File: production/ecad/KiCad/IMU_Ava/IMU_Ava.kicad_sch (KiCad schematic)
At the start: 0 parts

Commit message: add schematic, pullup resistors
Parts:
- added C1, C2: 100nF, Capacitor_SMD:C_0805_2012Metric_Pad1.18x1.45mm_HandSolder, symbol Device:C_Small
- added J1: Conn_01x04_Socket, Connector_JST:JST_EH_B4B-EH-A_1x04_P2.50mm_Vertical, symbol Connector:Conn_01x04_Socket
- added R1, R2, R3, R4: 10k, Resistor_SMD:R_0805_2012Metric_Pad1.20x1.40mm_HandSolder, symbol Device:R_Small_US
- added TP1, TP2: ~, TestPoint:TestPoint_Pad_D1.5mm, symbol Connector:TestPoint
- added U1: BMI088, BMI088:PQFN50P450X300X100-16N, symbol BMI088:BMI088
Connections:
- new net: R1.1, U1.10 (SDO2)
- new net: R4.2, U1.14 (CSB1)
- new net: R2.1, U1.15 (SDO1)
- new net: R3.2, U1.7 (PS)
- new net +3.3V: C1.1, C2.1, J1.4 (Pin_4), R3.1, R4.1, U1.11 (VDDIO), U1.3 (VDD)
- new net GND: C1.2, C2.2, J1.1 (Pin_1), R1.2, R2.2, U1.2 (NC), U1.4 (GNDA), U1.6 (GNDIO)
- new net SCL: J1.3 (Pin_3), TP1.1, U1.8 (SCL/SCK)
- new net SDA: J1.2 (Pin_2), TP2.1, U1.9 (SDA/SDI)
- no-connect marks 0 -> 5
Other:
- note added: "male conn 4 pos"

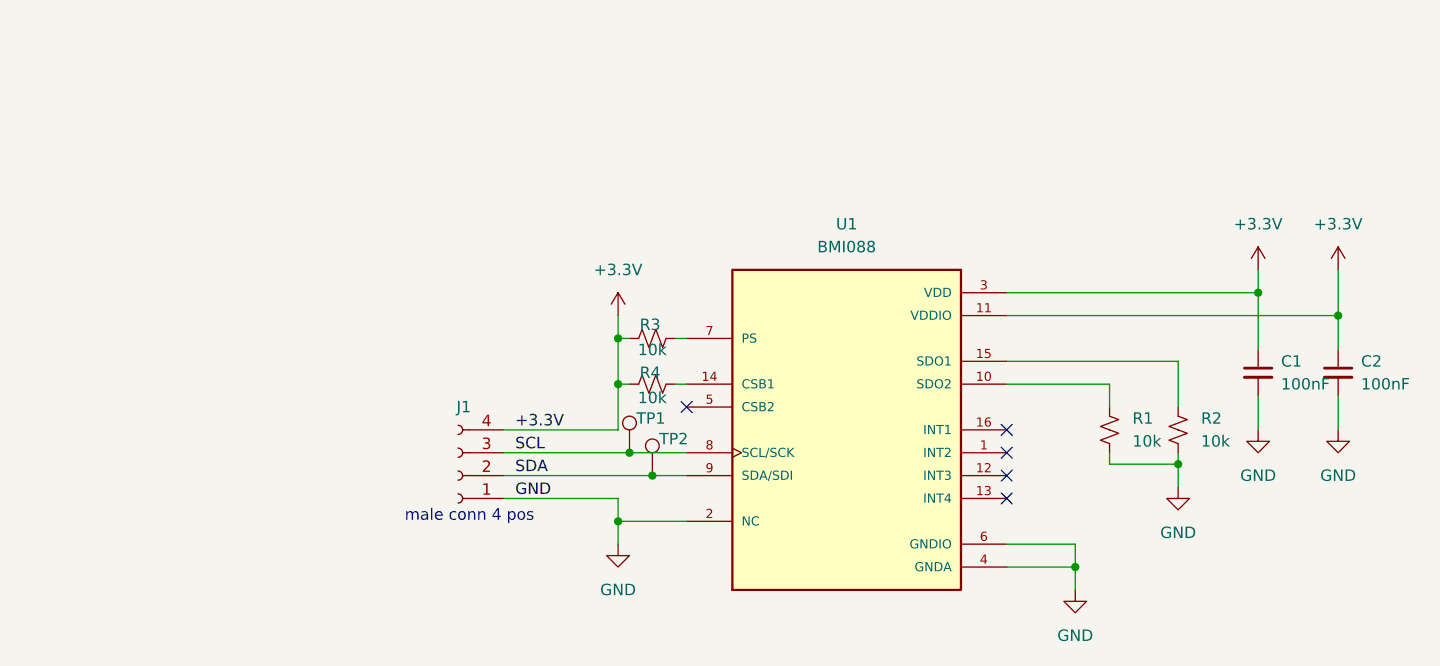
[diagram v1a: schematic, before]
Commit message: IMU 90 deg conn, fixes
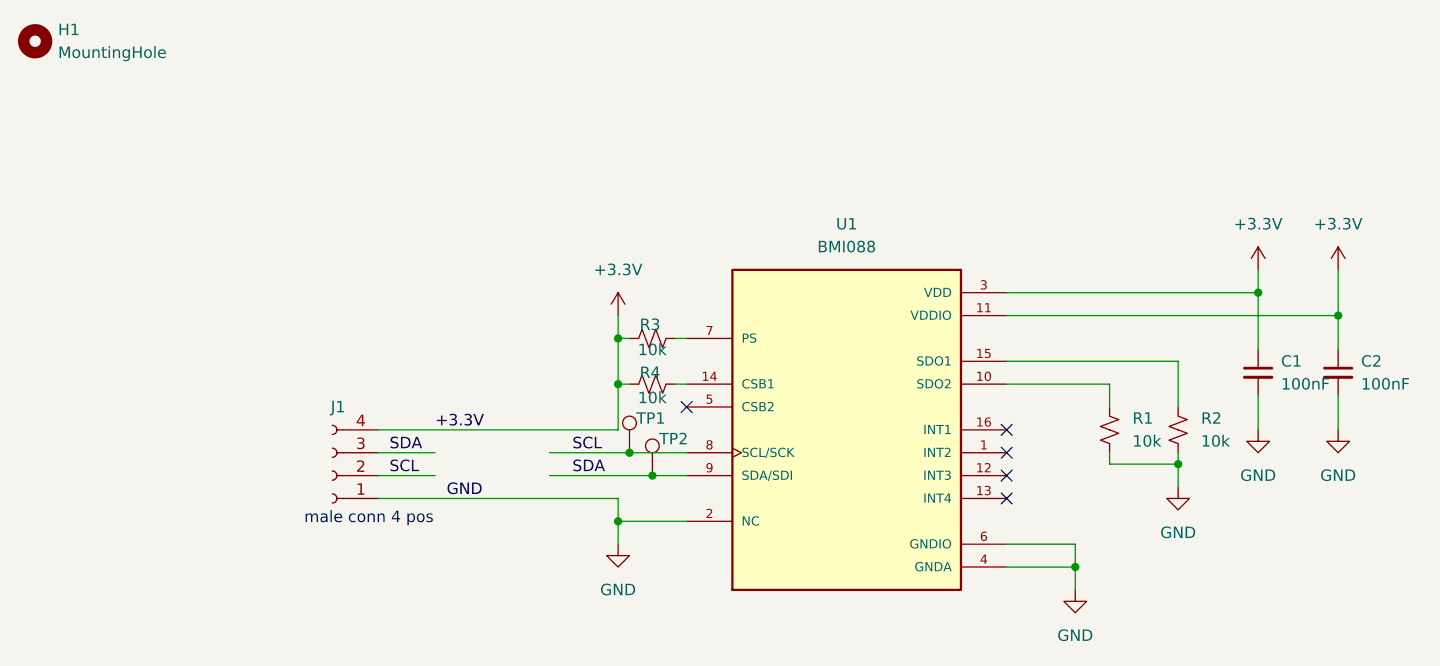
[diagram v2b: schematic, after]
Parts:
- added H1: MountingHole, symbol Mechanical:MountingHole
- J1: footprint Connector_JST:JST_EH_B4B-EH-A_1x04_P2.50mm_Vertical -> Connector_JST:JST_EH_S4B-EH_1x04_P2.50mm_Horizontal
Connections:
- net SCL: now also J1.2 (Pin_2); no longer J1.3 (Pin_3)
- net SDA: now also J1.3 (Pin_3); no longer J1.2 (Pin_2)
